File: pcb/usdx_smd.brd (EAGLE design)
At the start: 160 x 100 mm, 70 parts, among them IC1 MEGA8-AI, IC2 TL072P, IC4 REG1117, IC5 REG1117, IC6 74ACT00N, J2 JW-PJ-307-3, J3 JW-PJ-307-3, Q1 BS170, Q2 BS170, Q3 BS170, SW1 EC12E_SW, U1 Si5351A-B-GT, X1 1-227161-7, X2 27MHz, X3 CRYSTALS-NOGND-HC49

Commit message: Schematics maybe complete.
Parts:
- added C24: (no value), rcl:CT7343
- added C25: 10n, rcl:C1206K
- added C26: 100n, rcl:C0603K
- added R26: 470, rcl:M1206
- added R27, R28, R29: 10k, rcl:M1206
- J2, J3: value JW-PJ-307-3 -> JW-PJ-307-5
- moved J3 724.4 mm to (-127.0, -633.7)
- moved J2 699.6 mm to (-102.9, -633.7)
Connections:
- new net +5V_A: R29.2
- new net AUDIO_OUT: IC1.13, R26.1
- new net MIC_IN: IC1.16
- new net N$28: C26.2, R27.2, R28.1
- new net N$32: C25.2, C26.1, J3.P$4, J3.P$5, R29.1
- new net N$33: C24.-, J2.P$2, J2.P$3, J2.P$4, J2.P$5
- new net N$35: C24.+, R26.2
- new net PTT: IC1.17, J3.P$2, J3.P$3
- net AREF: now also R27.1
- net GND: now also C25.1, J2.P$1, J3.P$1, R28.2
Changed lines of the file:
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@@
 <element name="R11" library="rcl" package="M1206" value="10k" x="-72.39" y="-317.5"/>
 <element name="R12" library="rcl" package="M1206" value="10k" x="-72.39" y="-325.12"/>
-<element name="J2" library="audioconn" package="JW-PJ-307-X" value="JW-PJ-307-3" x="120.65" y="29.21"/>
-<element name="J3" library="audioconn" package="JW-PJ-307-X" value="JW-PJ-307-3" x="120.65" y="46.99"/>
 <element name="JP1" library="pinhead" package="1X04" value="" x="-63.5" y="-336.55"/>
 <element name="JP2" library="pinhead" package="1X04" value="" x="-63.5" y="-351.79"/>
@@
 <element name="C22" library="rcl" package="E5-13" value="" x="-72.39" y="-626.11"/>
 <element name="C23" library="rcl" package="CT7343" value="" x="-80.01" y="-643.89"/>
+<element name="J2" library="audioconn" package="JW-PJ-307-X" value="JW-PJ-307-5" x="-102.87" y="-633.73"/>
+<element name="J3" library="audioconn" package="JW-PJ-307-X" value="JW-PJ-307-5" x="-127" y="-633.73"/>
+<element name="C24" library="rcl" package="CT7343" value="" x="-128.27" y="-651.51"/>
+<element name="R26" library="rcl" package="M1206" value="470" x="-133.35" y="-657.86"/>
+<element name="R27" library="rcl" package="M1206" value="10k" x="-133.35" y="-665.48"/>
+<element name="R28" library="rcl" package="M1206" value="10k" x="-133.35" y="-673.1"/>
+<element name="R29" library="rcl" package="M1206" value="10k" x="-133.35" y="-680.72"/>
+<element name="C25" library="rcl" package="C1206K" value="10n" x="-133.35" y="-688.34"/>
+<element name="C26" library="rcl" package="C0603K" value="100n" x="-133.35" y="-694.69"/>
 </elements>
 <signals>
@@
 <contactref element="J1" pad="3"/>
 <contactref element="C23" pad="-"/>
+<contactref element="J2" pad="P$1"/>
+<contactref element="J3" pad="P$1"/>
+<contactref element="R28" pad="2"/>
+<contactref element="C25" pad="1"/>
 <wire x1="189.625" y1="66.04" x2="190.5" y2="61.8031" width="0" layer="19" extent="1-1"/>
 <wire x1="145.655" y1="72.39" x2="189.625" y2="66.04" width="0" layer="19" extent="1-1"/>
@@
 <wire x1="-69.85" y1="-626.11" x2="-85.485" y2="-610.87" width="0" layer="19" extent="1-1"/>
 <wire x1="-76.81" y1="-643.89" x2="-69.85" y2="-626.11" width="0" layer="19" extent="1-1"/>
+<wire x1="-99.87" y1="-631.23" x2="-85.485" y2="-610.87" width="0" layer="19" extent="1-1"/>
+<wire x1="-124" y1="-631.23" x2="-99.87" y2="-631.23" width="0" layer="19" extent="1-1"/>
+<wire x1="-131.95" y1="-673.1" x2="-124" y2="-631.23" width="0" layer="19" extent="1-1"/>
+<wire x1="-134.85" y1="-688.34" x2="-131.95" y2="-673.1" width="0" layer="19" extent="1-1"/>
 </signal>
 <signal name="+5V">
@@
 <contactref element="R11" pad="2"/>
 <contactref element="IC1" pad="20"/>
+<contactref element="R27" pad="1"/>
 <wire x1="-70.99" y1="-302.26" x2="-70.99" y2="-317.5" width="0" layer="19" extent="1-1"/>
+<wire x1="-134.75" y1="-665.48" x2="-70.99" y2="-317.5" width="0" layer="19" extent="1-1"/>
 <wire x1="64.2874" y1="69.45" x2="-70.99" y2="-302.26" width="0" layer="19" extent="1-16"/>
 </signal>
@@
 <wire x1="50.165" y1="29.845" x2="43.815" y2="31.115" width="0" layer="19" extent="1-1"/>
 </signal>
+<signal name="N$32">
+<contactref element="J3" pad="P$4"/>
+<contactref element="J3" pad="P$5"/>
+<contactref element="R29" pad="1"/>
+<contactref element="C25" pad="2"/>
+<contactref element="C26" pad="1"/>
+<wire x1="-129" y1="-633.23" x2="-124" y2="-638.73" width="0" layer="19" extent="1-1"/>
+<wire x1="-134.75" y1="-680.72" x2="-124" y2="-638.73" width="0" layer="19" extent="1-1"/>
+<wire x1="-131.85" y1="-688.34" x2="-134.75" y2="-680.72" width="0" layer="19" extent="1-1"/>
+<wire x1="-134.225" y1="-694.69" x2="-131.85" y2="-688.34" width="0" layer="19" extent="1-1"/>
+</signal>
+<signal name="N$33">
+<contactref element="J2" pad="P$2"/>
+<contactref element="J2" pad="P$3"/>
+<contactref element="J2" pad="P$4"/>
+<contactref element="J2" pad="P$5"/>
+<contactref element="C24" pad="-"/>
+<wire x1="-99.87" y1="-636.23" x2="-99.87" y2="-638.73" width="0" layer="19" extent="1-1"/>
+<wire x1="-104.87" y1="-633.23" x2="-99.87" y2="-636.23" width="0" layer="19" extent="1-1"/>
+<wire x1="-99.87" y1="-628.73" x2="-104.87" y2="-633.23" width="0" layer="19" extent="1-1"/>
+<wire x1="-125.07" y1="-651.51" x2="-104.87" y2="-633.23" width="0" layer="19" extent="1-1"/>
+</signal>
+<signal name="N$35">
+<contactref element="C24" pad="+"/>
+<contactref element="R26" pad="2"/>
+<wire x1="-131.47" y1="-651.51" x2="-131.95" y2="-657.86" width="0" layer="19" extent="1-1"/>
+</signal>
+<signal name="AUDIO_OUT">
+<contactref element="R26" pad="1"/>
+<contactref element="IC1" pad="13"/>
+<wire x1="-134.75" y1="-657.86" x2="68.18" y2="65.5574" width="0" layer="19" extent="1-16"/>
+</signal>
+<signal name="PTT">
+<contactref element="IC1" pad="17"/>
+<contactref element="J3" pad="P$2"/>
+<contactref element="J3" pad="P$3"/>
+<wire x1="-124" y1="-628.73" x2="-124" y2="-636.23" width="0" layer="19" extent="1-1"/>
+<wire x1="64.2874" y1="67.05" x2="-124" y2="-628.73" width="0" layer="19" extent="16-16"/>
+</signal>
+<signal name="MIC_IN">
+<contactref element="IC1" pad="16"/>
+</signal>
+<signal name="N$28">
+<contactref element="R27" pad="2"/>
+<contactref element="R28" pad="1"/>
+<contactref element="C26" pad="2"/>
+<wire x1="-134.75" y1="-673.1" x2="-132.475" y2="-694.69" width="0" layer="19" extent="1-1"/>
+<wire x1="-131.95" y1="-665.48" x2="-134.75" y2="-673.1" width="0" layer="19" extent="1-1"/>
+</signal>
+<signal name="+5V_A">
+<contactref element="R29" pad="2"/>
+</signal>
 </signals>

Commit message: Schematics 99%, placing started.
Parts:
- removed U$1: FST3253, FST3253:TSSOP16
- removed U1: Si5351A-B-GT, microbuilder:MSOP10
- added C27: 100n, rcl:C0603K
- added C28, C29: 10n, rcl:C0603K
- added IC3: REG1117, burr-brown:SOT223
- added IC7: 74ACT00N, 74xx-eu:DIL14
- added Q4: BS170, transistor-small-signal:SOT54E
- added R30: 1k, rcl:R1206
- C5: value (none) -> 10n
- IC2: value TL072P -> REG1117; device linear:DIL08 -> burr-brown:SOT223
- IC4: value REG1117 -> Si5351A-B-GT; device burr-brown:SOT223 -> microbuilder:MSOP10
- IC5: value REG1117 -> FST3253; device burr-brown:SOT223 -> FST3253:TSSOP16
- IC6: value 74ACT00N -> TL072P; device 74xx-eu:DIL14 -> linear:DIL08
- R22: value 1k -> FB; device rcl:M1206 -> rcl:R1206
- moved C26 762.7 mm to (118.1, 25.4)
- moved C25 760.5 mm to (125.7, 26.7)
- moved R28 757.2 mm to (119.4, 40.6)
- moved R29 754.8 mm to (119.4, 30.5)
- moved R26 753.6 mm to (119.4, 52.1)
- moved C24 749.3 mm to (129.5, 52.1)
- moved R27 745.2 mm to (119.4, 35.6)
- moved J2 734.5 mm to (128.3, 63.5), turned to 180 degrees
- moved J3 717.5 mm to (128.3, 36.8), turned to 180 degrees
- moved C23 668.3 mm to (128.3, -8.89)
- moved C19 661.5 mm to (27.9, 80.0)
- moved C21 657.1 mm to (128.3, 10.2)
- moved R21 656.3 mm to (35.6, 80.0)
- moved R25 652.8 mm to (86.4, 29.2)
- moved R24 651.6 mm to (104.1, 30.5)
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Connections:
- removed net N$20: C17.1
- new net N$31: IC1.18, R22.2
- new net RXS: C17.1, Q4.S, R30.2
- net +3V3: now also IC3.2, IC4.1, IC4.7; no longer IC5.2, U1.1, U1.7
- net +5V: now also C27.1, IC2.2, IC3.3, IC5.16, IC6.8, IC7.12, IC7.13, IC7.14, R22.1; no longer IC1.18, IC2.8, IC4.2, IC5.3, IC6.12, IC6.13, IC6.14, U$1.16
- net CLK0: now also IC4.10, IC5.14; no longer U$1.14, U1.10
- net CLK1: now also IC4.9, IC5.2; no longer U$1.2, U1.9
- net CLK2: now also IC4.6, IC7.5; no longer IC6.5, U1.6
- net GND: now also C27.2, C28.1, IC2.1, IC3.1, IC4.8, IC5.15, IC5.8, IC6.4, IC7.7, R30.1; no longer IC2.4, IC4.1, IC6.7, U$1.1, U$1.15, U$1.8, U1.8
- net N$10: now also IC6.5; no longer IC2.5
- net N$11: now also IC6.6; no longer IC2.6
- net N$14: now also IC5.12; no longer U$1.12
- net N$15: now also IC5.11; no longer U$1.11
- net N$16: now also IC6.1; no longer IC2.1
- net N$17: now also IC5.13; no longer U$1.13
- net N$18: now also IC6.7; no longer IC2.7
- net N$19: now also IC5.10; no longer U$1.10
- net N$2: now also C29.1, Q4.D; no longer IC6.1, IC6.2
- net N$25: now also IC5.9; no longer U$1.7
- net N$3: now also IC6.3; no longer IC2.3
- net N$4: now also IC4.3; no longer U1.3
- net N$5: now also IC4.2; no longer U1.2
- net N$6: now also IC7.3, IC7.4; no longer IC6.3, IC6.4
- net N$7: now also IC7.10, IC7.6, IC7.9; no longer IC6.10, IC6.6, IC6.9
- net N$8: now also IC6.2; no longer IC2.2
- net N$9: now also IC7.8; no longer IC6.8
- net RD: now also C29.2
- net SCL: now also IC4.4; no longer U1.4
- net SDA: now also IC4.5; no longer U1.5
- net TX: now also C28.2, IC1.12, IC7.1, IC7.2, Q4.G
- net VCC: now also IC2.3; no longer IC4.3
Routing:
- net N$10: track 0.00 -> 24.8 mm
- net GND: track 0.00 -> 20.0 mm, vias 0 -> 4
- net N$14: track 0.00 -> 17.9 mm
- net N$15: track 0.00 -> 16.3 mm
- net +5V: track 0.00 -> 15.2 mm
- net N$11: track 0.00 -> 14.0 mm
- net N$17: track 0.00 -> 13.6 mm
- net TD: track 0.00 -> 10.3 mm
- net N$1: track 0.00 -> 10.3 mm
- net N$7: track 0.00 -> 10.2 mm
- net N$19: track 0.00 -> 9.25 mm
- net N$8: track 0.00 -> 7.43 mm
- net N$3: track 0.00 -> 6.64 mm
- net TX: track 0.00 -> 2.54 mm
- net N$6: track 0.00 -> 2.54 mm
- added copper zone on layer 16, net GND
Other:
- board size 160 x 100 mm -> 127 x 63 mm

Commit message: More routing
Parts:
- moved C18 60.0 mm to (37.6, -23.8), turned to 90 degrees
- moved R15 55.5 mm to (40.0, -23.7), turned to 270 degrees
- moved C17 51.6 mm to (51.1, -21.9), turned to 90 degrees
- moved R16 46.9 mm to (47.5, -23.8), turned to 270 degrees
- moved R14 45.4 mm to (43.5, -23.7)
- moved C11 11.4 mm to (58.1, -19.2), flipped to the bottom, turned to 180 degrees
- moved C12 10.6 mm to (58.1, -22.4), flipped to the bottom, turned to 180 degrees
- moved C13 8.01 mm to (58.1, -16.0), flipped to the bottom, turned to 180 degrees
- moved C14 7.79 mm to (58.1, -25.6), flipped to the bottom, turned to 180 degrees
- moved R1 3.18 mm to (58.1, -22.4)
- moved R6 3.18 mm to (58.1, -25.6)
- moved R4 3.17 mm to (58.1, -19.2)
- moved R5 3.17 mm to (58.1, -16.0)
- moved C7 2.21 mm to (48.3, -17.6)
- moved IC5 2.21 mm to (48.3, -17.6)
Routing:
- net GND: track 20.0 -> 34.0 mm, vias 4 -> 1
- net N$14: track 17.9 -> 6.28 mm, vias 0 -> 1
- net N$15: track 16.3 -> 7.27 mm, vias 0 -> 1
- net N$10: track 24.8 -> 17.2 mm
- net N$17: track 13.6 -> 6.27 mm, vias 0 -> 1
- net N$11: track 14.0 -> 20.4 mm
- net +5V: track 15.2 -> 18.8 mm, vias 0 -> 1
- net N$8: track 7.43 -> 6.11 mm
- net N$19: track 9.25 -> 10.2 mm, vias 0 -> 1
- net N$3: track 6.64 -> 5.85 mm

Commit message: Much much routing
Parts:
- removed J1: (no value), con-jack:DCJ0303
- removed JP2: (no value), pinhead:1X04
- removed R20: 10k, rcl:RTRIMT93YA
- added C30: 100n, rcl:C0603K
- added C31: (no value), rcl:C0603K
- added CF1-A, CF1-B, CF2-A, CF2-B, CF3-A, CF3-B, CF4-A, CF4-B, CF5-A, CF5-B, CF6-A, CF6-B: (no value), rcl:C025-024X044
- added H1, H2, H3, H4: MOUNT-PAD-ROUND3.2, holes:3,2-PAD
- added JP3, JP4: (no value), pinhead:1X02
- added K1, K2: TQ2SA-L2-5V, relay:TQ-SA
- added L1-A, L1-B, L2-A, L2-B: T37, inductor:T37
- added R31, R32, R33, R34: 1k, rcl:R1206
- added R35: 1k, rcl:M1206
- added R36: (no value), rcl:RTRIM3374
- added T1, T2: (no value), transistor:SOT23-EBC
- added U$5: FT37-43, inductor:T37
- C17, C28, C29: device rcl:C0603K -> rcl:C1206K
- JP1: device pinhead:1X04 -> pinhead:2X03
- X1: value 1-227161-7 -> BU-SMA-H; device con-coax:AMP_227161 -> con-coax:BU-SMA-H
- moved R2 150.3 mm to (56.2, 37.8), turned to 270 degrees
- moved X2 136.5 mm to (55.2, 50.2), turned to 0 degrees
- moved R3 133.8 mm to (52.4, 37.8), turned to 270 degrees
- moved C1 127.5 mm to (64.5, 46.7), turned to 0 degrees
- moved IC4 127.4 mm to (64.1, 43.5), turned to 270 degrees
- moved C28 118.9 mm to (87.5, 20.5), flipped to the bottom, turned to 270 degrees
- moved C29 107.5 mm to (72.9, 12.7)
- moved R30 101.0 mm to (72.9, 6.35), turned to 180 degrees
- moved Q4 95.1 mm to (71.6, 20.3)
- moved C16 87.8 mm to (2.54, 38.1)
- moved R23 80.8 mm to (17.1, 59.1)
- moved C18 79.0 mm to (112.2, 2.22), turned to 180 degrees
- moved R15 77.7 mm to (112.2, 5.08), turned to 0 degrees
- moved C15 76.2 mm to (10.2, 38.1)
- moved R14 75.9 mm to (112.2, 8.57), turned to 180 degrees
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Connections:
- removed net +12V: JP2.1
- removed net N$28: C26.2, R27.2, R28.1
- removed net N$35: C24.+, R26.2
- removed net RD: C29.2, JP2.3
- removed net TD: Q1.D, Q2.D, Q3.D
- new net AVCC: C6.1, IC1.18, R22.2
- new net MOSI: IC1.15, JP1.4
- new net N$20: K1.6, K2.6, T1.C
- new net N$34: JP3.1, JP4.2
- new net N$36: R31.1, T1.B
- new net N$37: R32.1, T2.B
- new net N$40: K1.3, X1.1
- new net N$44: K2.8
- new net N$46: CF5-A.1, CF6-A.1, K1.4, K1.9, L2-A.P$1
- new net N$47: CF2-A.2, CF3-A.2, CF4-A.2, CF5-A.2, L2-A.P$2
- new net N$48: CF5-B.1, CF6-B.1, K1.2, K1.7, L2-B.P$1
- new net N$49: CF2-B.2, CF3-B.2, CF4-B.2, CF5-B.2, L2-B.P$2
- new net N$50: CF2-B.1, CF3-B.1, L1-B.P$1
- new net N$51: CF2-A.1, CF3-A.1, L1-A.P$1
- new net N$52: CF1-A.1, K2.2, K2.7, L1-A.P$2
- new net N$53: CF1-B.1, K2.4, K2.9, L1-B.P$2
- new net PC2: IC1.25
- new net PD5: IC1.9
- new net RELAY1: IC1.19, R31.2, R34.1
- new net RELAY2: IC1.22, R32.2, R33.1
- new net SS: IC1.14
- new net TRD: C29.2, Q1.D, Q2.D, Q3.D, U$5.P$1
- net +5V: now also JP1.2, K1.1, K1.10, K2.1, K2.10, R35.1; no longer C6.1
- net +5V_A: now also C31.1, R35.2
- net AUDIO_OUT: now also C24.+; no longer R26.1
- net GND: now also C30.2, C31.2, CF1-A.2, CF1-B.2, CF4-A.1, CF4-B.1, CF6-A.2, CF6-B.2, JP1.6, JP4.1, K1.8, K2.3, R33.2, R34.2, T1.E, T2.E, X1.3, X1.4, X1.5; no longer J1.2, J1.3, JP1.1, JP1.2, JP2.4
- net LCD_CONTR: now also R36.2; no longer R20.2
- net LCD_VCC: now also R36.1; no longer R20.3
- net MIC_IN: now also C26.2, JP1.1, R27.2, R28.1
- net N$22: now also K1.5, K2.5, T2.C; no longer JP1.3, JP1.4, X1.1
- net N$27: now also R36.3; no longer R20.1
- net N$31: now also C24.-, R26.1; no longer IC1.18, R22.2
- net N$33: now also R26.2; no longer C24.-
- net PTT: now also JP1.3
- net RESET: now also JP1.5
- net TX: no longer JP2.2
- net VCC: now also C30.1, JP3.2, U$5.P$2; no longer J1.1
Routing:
- net +5V: track 18.8 -> 310.8 mm
- net MIC_IN: track 0.00 -> 168.0 mm, vias 0 -> 2
- net VCC: track 0.00 -> 94.1 mm
- net TX: track 2.54 -> 89.0 mm, vias 0 -> 5
- net BUTTONS: track 0.00 -> 75.3 mm, vias 0 -> 1
- net AUDIO_OUT: track 0.00 -> 73.6 mm, vias 0 -> 3
- net N$20: track 0.00 -> 67.6 mm, vias 0 -> 2
- net N$32: track 0.00 -> 66.3 mm
- net N$22: track 0.00 -> 65.5 mm, vias 0 -> 3
- net N$18: track 0.00 -> 62.5 mm, vias 0 -> 2
- net N$16: track 0.00 -> 57.5 mm, vias 0 -> 2
- net RXS: track 0.00 -> 54.1 mm
- net SCL: track 0.00 -> 48.6 mm, vias 0 -> 3
- net +3V3: track 0.00 -> 47.2 mm
- net RESET: track 0.00 -> 45.9 mm, vias 0 -> 1
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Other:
- board size 127 x 63 mm -> 126 x 67 mm

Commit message: More routing
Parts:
- moved R17 23.5 mm to (67.9, 63.8), turned to 180 degrees
- moved R18 23.2 mm to (72.4, 62.2), turned to 90 degrees
- moved R19 15.9 mm to (72.4, 56.8), turned to 90 degrees
- moved IC3 8.78 mm to (57.5, 59.1), turned to 90 degrees
- moved C4 7.05 mm to (63.5, 60.6), turned to 270 degrees
- moved X2 3.42 mm to (54.0, 47.0)
- moved C3 2.71 mm to (63.5, 57.5), turned to 90 degrees
- moved R22 2.25 mm to (22.2, 42.5)
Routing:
- net BUTTONS: track 75.3 -> 128.9 mm
- net SDA: track 23.3 -> 68.4 mm, vias 1 -> 3
- net LCD_VCC: track 2.67 -> 46.8 mm
- net N$18: track 62.5 -> 105.2 mm, vias 2 -> 4
- net N$16: track 57.5 -> 96.0 mm, vias 2 -> 4
- net AREF: track 14.1 -> 41.7 mm, vias 1 -> 2
- net N$24: track 3.02 -> 24.0 mm
- net +5V: track 310.8 -> 290.6 mm
- net VCC: track 94.1 -> 81.3 mm
- net AUDIO_OUT: track 73.6 -> 71.1 mm
- net N$5: track 9.26 -> 6.87 mm
- net SCL: track 48.6 -> 50.9 mm
- net MIC_IN: track 168.0 -> 165.8 mm
- net N$4: track 13.1 -> 11.9 mm
- net N$21: track 4.28 -> 3.12 mm
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
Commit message: Some more routing
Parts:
- moved R2 1.91 mm to (56.2, 39.7)
- moved R3 1.91 mm to (52.4, 39.7)
- moved C9 1.59 mm to (103.3, 34.3)
- moved C10 1.27 mm to (105.9, 25.4)
- moved IC6 1.27 mm to (103.3, 25.4)
- moved C8 1.27 mm to (95.2, 25.1)
- moved R24 1.27 mm to (111.4, 27.3)
- moved R7 1.27 mm to (98.1, 25.1)
- moved R8 1.27 mm to (103.3, 32.1)
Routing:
- net AREF: track 41.7 -> 138.4 mm, vias 2 -> 6
- net N$16: track 96.0 -> 122.9 mm, vias 4 -> 5
- net N$18: track 105.2 -> 131.8 mm
- net +5V: track 290.6 -> 272.5 mm
- net SCL: track 50.9 -> 48.0 mm
- net SDA: track 68.4 -> 65.9 mm
- net BUTTONS: track 128.9 -> 126.8 mm
- net N$11: track 25.3 -> 23.8 mm
- net N$29: track 9.29 -> 10.6 mm
- net N$3: track 5.85 -> 4.58 mm
- net N$8: track 16.2 -> 14.9 mm
- net +3V3: track 47.1 -> 46.3 mm
- net N$10: track 17.2 -> 16.6 mm

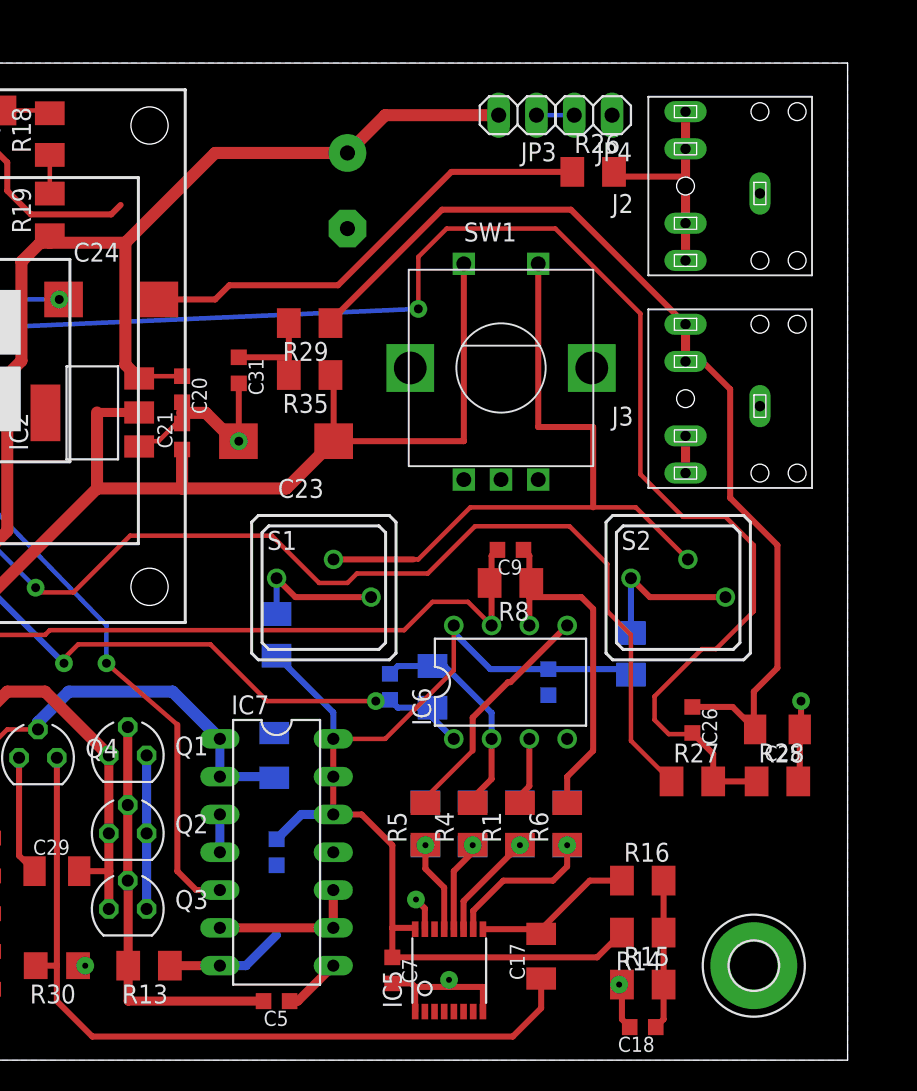
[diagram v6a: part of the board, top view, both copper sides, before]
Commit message: And more routing
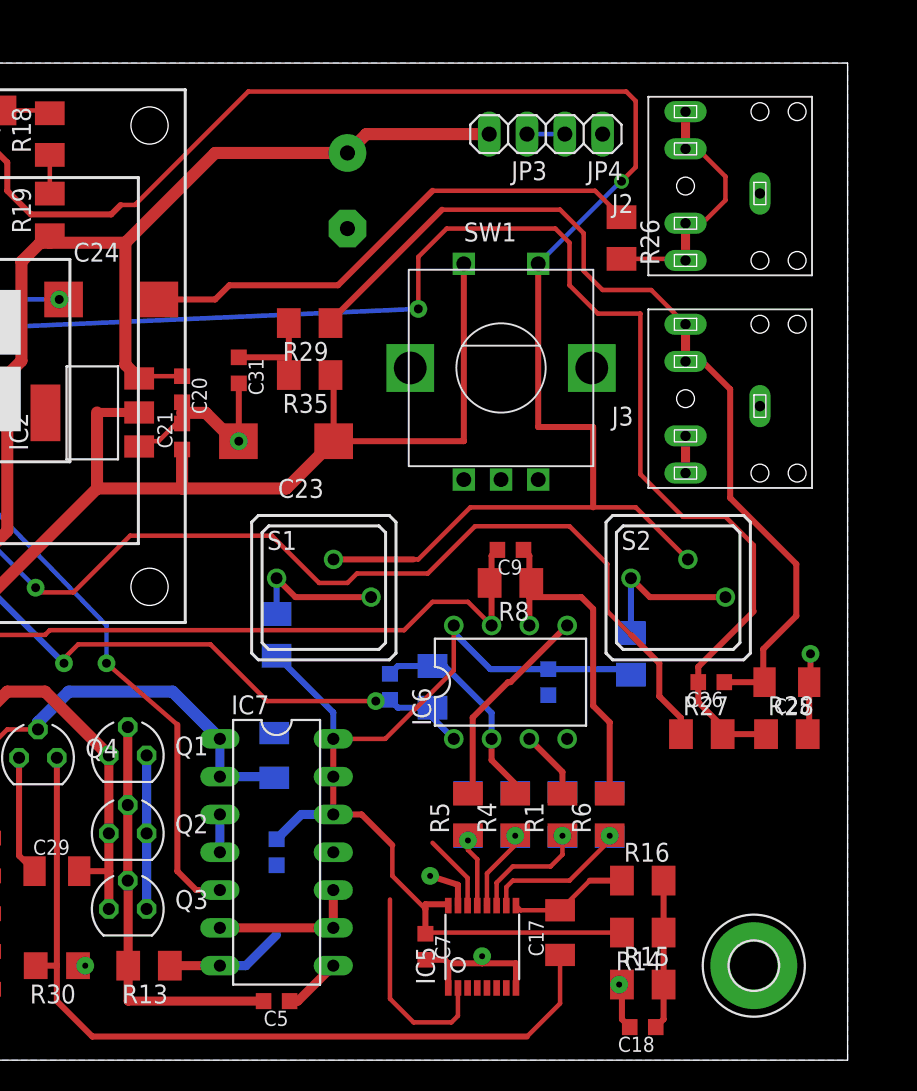
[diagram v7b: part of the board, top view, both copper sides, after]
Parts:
- moved R26 4.84 mm to (110.8, 55.2), turned to 270 degrees
- moved C25 3.24 mm to (121.9, 25.4)
- moved R27 3.24 mm to (116.2, 21.9)
- moved R28 3.24 mm to (121.9, 21.9)
- moved C12 2.93 mm to (106.8, 16.5)
- moved C13 2.93 mm to (100.5, 16.5)
- moved C14 2.93 mm to (110.0, 16.5)
- moved R1 2.93 mm to (106.8, 16.5)
- moved R5 2.93 mm to (100.5, 16.5)
- moved R6 2.93 mm to (110.0, 16.5)
- moved C11 2.93 mm to (103.7, 16.5)
- moved R4 2.93 mm to (103.7, 16.5)
- moved C26 2.84 mm to (116.8, 25.4), turned to 180 degrees
- moved C7 2.73 mm to (97.6, 7.62)
- moved IC5 2.73 mm to (101.4, 7.62)
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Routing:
- net BUTTONS: track 126.8 -> 178.5 mm, vias 1 -> 2
- net CLK1: track 0.00 -> 13.9 mm
- net MIC_IN: track 165.8 -> 160.5 mm
- net CLK0: track 0.00 -> 5.19 mm
- net N$31: track 31.3 -> 34.9 mm
- net +5V: track 272.5 -> 269.3 mm
- net N$32: track 66.3 -> 63.2 mm
- net N$25: track 11.0 -> 8.08 mm
- net AREF: track 138.4 -> 135.5 mm
- net N$33: track 14.9 -> 17.7 mm
- net RXS: track 54.1 -> 56.8 mm
- net N$10: track 16.6 -> 14.2 mm
- net VCC: track 81.3 -> 80.1 mm
- net GND: track 76.3 -> 77.4 mm
- net N$17: track 6.27 -> 5.23 mm
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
